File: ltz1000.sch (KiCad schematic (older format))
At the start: 62 parts, among them Q1 ZTX851, U11 ADA4522-2, U24 LT6018, U25 ADA4522-2, U26 ADA4522-1, U27 OPA140, U28 OPA140, U29 OPA140, U30 OPA140

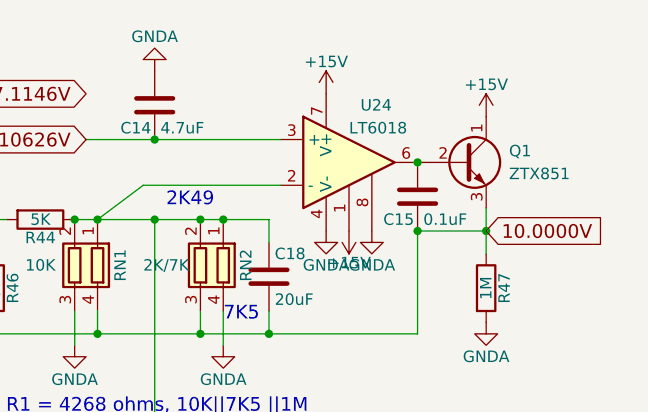
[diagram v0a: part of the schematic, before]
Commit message: Add files via upload
Updated opamps to ada4522 because they have lower bias current.
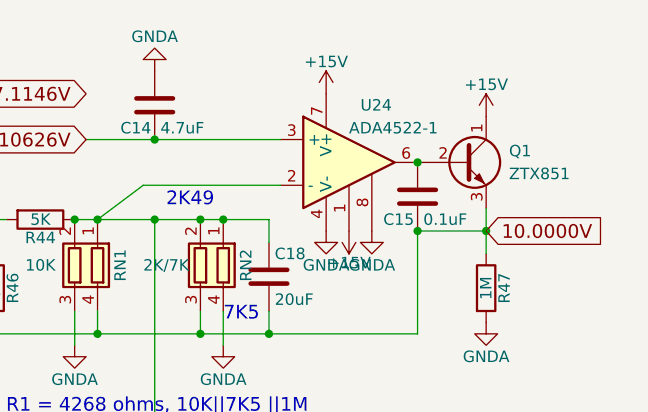
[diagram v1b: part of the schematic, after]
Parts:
- U24: value LT6018 -> ADA4522-1
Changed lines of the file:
@@
 $Descr A4 11693 8268
 encoding utf-8
-Sheet 2 5
+Sheet 2 6
 Title "DIY Differential Voltmeter.  Version 1"
 Date "2019-05-20"
@@
 NoConn ~ 2750 4800
 $Comp
-L GNDA #PWR64
+L GNDA #PWR045
 U 1 1 5B84AD0F
 P 2250 4700
-F 0 "#PWR64" H 2250 4450 50  0001 C CNN
+F 0 "#PWR045" H 2250 4450 50  0001 C CNN
 F 1 "GNDA" H 2250 4550 50  0000 C CNN
 F 2 "" H 2250 4700 50  0001 C CNN
@@
 $EndComp
 $Comp
-L +15V #PWR62
+L +15V #PWR046
 U 1 1 5B84B928
 P 2650 4200
-F 0 "#PWR62" H 2650 4050 50  0001 C CNN
+F 0 "#PWR046" H 2650 4050 50  0001 C CNN
 F 1 "+15V" H 2650 4340 50  0000 C CNN
 F 2 "" H 2650 4200 50  0001 C CNN
@@
 NoConn ~ 2750 6350
 $Comp
-L GNDA #PWR69
+L GNDA #PWR047
 U 1 1 5B84E7A7
 P 2250 6250
-F 0 "#PWR69" H 2250 6000 50  0001 C CNN
+F 0 "#PWR047" H 2250 6000 50  0001 C CNN
 F 1 "GNDA" H 2250 6100 50  0000 C CNN
 F 2 "" H 2250 6250 50  0001 C CNN
@@
 $EndComp
 $Comp
-L +15V #PWR67
+L +15V #PWR048
 U 1 1 5B84E7AE
 P 2650 5750
-F 0 "#PWR67" H 2650 5600 50  0001 C CNN
+F 0 "#PWR048" H 2650 5600 50  0001 C CNN
 F 1 "+15V" H 2650 5890 50  0000 C CNN
 F 2 "" H 2650 5750 50  0001 C CNN
@@
 NoConn ~ 6400 4700
 $Comp
-L GNDA #PWR63
+L GNDA #PWR049
 U 1 1 5B84EA99
 P 5900 4600
-F 0 "#PWR63" H 5900 4350 50  0001 C CNN
+F 0 "#PWR049" H 5900 4350 50  0001 C CNN
 F 1 "GNDA" H 5900 4450 50  0000 C CNN
 F 2 "" H 5900 4600 50  0001 C CNN
@@
 $EndComp
 $Comp
-L +15V #PWR61
+L +15V #PWR050
 U 1 1 5B84EAA0
 P 6300 4100
-F 0 "#PWR61" H 6300 3950 50  0001 C CNN
+F 0 "#PWR050" H 6300 3950 50  0001 C CNN
 F 1 "+15V" H 6300 4240 50  0000 C CNN
 F 2 "" H 6300 4100 50  0001 C CNN
@@
 NoConn ~ 6400 6400
 $Comp
-L GNDA #PWR70
+L GNDA #PWR051
 U 1 1 5B84EADB
 P 5900 6300
-F 0 "#PWR70" H 5900 6050 50  0001 C CNN
+F 0 "#PWR051" H 5900 6050 50  0001 C CNN
 F 1 "GNDA" H 5900 6150 50  0000 C CNN
 F 2 "" H 5900 6300 50  0001 C CNN
@@
 $EndComp
 $Comp
-L +15V #PWR68
+L +15V #PWR052
 U 1 1 5B84EAE2
 P 6300 5800
-F 0 "#PWR68" H 6300 5650 50  0001 C CNN
+F 0 "#PWR052" H 6300 5650 50  0001 C CNN
 F 1 "+15V" H 6300 5940 50  0000 C CNN
 F 2 "" H 6300 5800 50  0001 C CNN
@@
 $EndComp
 $Comp
-L GNDA #PWR50
+L GNDA #PWR053
 U 1 1 5B92B409
 P 1750 1750
-F 0 "#PWR50" H 1750 1500 50  0001 C CNN
+F 0 "#PWR053" H 1750 1500 50  0001 C CNN
 F 1 "GNDA" H 1750 1600 50  0000 C CNN
 F 2 "" H 1750 1750 50  0001 C CNN
@@
 $EndComp
 $Comp
-L GNDA #PWR53
+L GNDA #PWR054
 U 1 1 5B92B41E
 P 4250 1850
-F 0 "#PWR53" H 4250 1600 50  0001 C CNN
+F 0 "#PWR054" H 4250 1600 50  0001 C CNN
 F 1 "GNDA" H 4250 1700 50  0000 C CNN
 F 2 "" H 4250 1850 50  0001 C CNN
@@
 $EndComp
 $Comp
-L GNDA #PWR51
+L GNDA #PWR055
 U 1 1 5B940C92
 P 2200 1850
-F 0 "#PWR51" H 2200 1600 50  0001 C CNN
+F 0 "#PWR055" H 2200 1600 50  0001 C CNN
 F 1 "GNDA" H 2200 1700 50  0000 C CNN
 F 2 "" H 2200 1850 50  0001 C CNN
@@
 $EndComp
 $Comp
-L +15V #PWR45
+L +15V #PWR056
 U 1 1 5B941207
 P 2200 1250
-F 0 "#PWR45" H 2200 1100 50  0001 C CNN
+F 0 "#PWR056" H 2200 1100 50  0001 C CNN
 F 1 "+15V" H 2200 1390 50  0000 C CNN
 F 2 "" H 2200 1250 50  0001 C CNN
@@
 $EndComp
 $Comp
-L +15V #PWR46
+L +15V #PWR057
 U 1 1 5B99A2E8
 P 6400 1250
-F 0 "#PWR46" H 6400 1100 50  0001 C CNN
+F 0 "#PWR057" H 6400 1100 50  0001 C CNN
 F 1 "+15V" H 6400 1390 50  0000 C CNN
 F 2 "" H 6400 1250 50  0001 C CNN
@@
 $EndComp
 $Comp
-L GNDA #PWR54
+L GNDA #PWR058
 U 1 1 5B99A3CA
 P 6400 1850
-F 0 "#PWR54" H 6400 1600 50  0001 C CNN
+F 0 "#PWR058" H 6400 1600 50  0001 C CNN
 F 1 "GNDA" H 6400 1700 50  0000 C CNN
 F 2 "" H 6400 1850 50  0001 C CNN
@@
 $EndComp
 $Comp
-L GNDA #PWR56
+L GNDA #PWR059
 U 1 1 5B99C24F
 P 5850 2200
-F 0 "#PWR56" H 5850 1950 50  0001 C CNN
+F 0 "#PWR059" H 5850 1950 50  0001 C CNN
 F 1 "GNDA" H 5850 2050 50  0000 C CNN
 F 2 "" H 5850 2200 50  0001 C CNN
@@
 $EndComp
 $Comp
-L GNDA #PWR59
+L GNDA #PWR060
 U 1 1 5B99E1F3
 P 5550 2600
-F 0 "#PWR59" H 5550 2350 50  0001 C CNN
+F 0 "#PWR060" H 5550 2350 50  0001 C CNN
 F 1 "GNDA" H 5550 2450 50  0000 C CNN
 F 2 "" H 5550 2600 50  0001 C CNN
@@
 $EndComp
 $Comp
-L GNDA #PWR52
+L GNDA #PWR061
 U 1 1 5BE3AEC6
 P 3850 1850
-F 0 "#PWR52" H 3850 1600 50  0001 C CNN
+F 0 "#PWR061" H 3850 1600 50  0001 C CNN
 F 1 "GNDA" H 3850 1700 50  0000 C CNN
 F 2 "" H 3850 1850 50  0001 C CNN
@@
 P 9600 1400
 F 0 "U24" H 9650 1650 50  0000 L CNN
-F 1 "LT6018" H 9600 1550 50  0000 L CNN
+F 1 "ADA4522-1" H 9600 1550 50  0000 L CNN
 F 2 "" H 9650 1450 50  0001 C CNN
 F 3 "" H 9650 1550 50  0001 C CNN
@@
 $EndComp
 $Comp
-L +15V #PWR43
+L +15V #PWR062
 U 1 1 5BEB7DD3
 P 9500 1100
-F 0 "#PWR43" H 9500 950 50  0001 C CNN
+F 0 "#PWR062" H 9500 950 50  0001 C CNN
 F 1 "+15V" H 9500 1240 50  0000 C CNN
 F 2 "" H 9500 1100 50  0001 C CNN
@@
 $EndComp
 $Comp
-L GNDA #PWR47
+L GNDA #PWR063
 U 1 1 5BEB7DD9
 P 9500 1700
-F 0 "#PWR47" H 9500 1450 50  0001 C CNN
+F 0 "#PWR063" H 9500 1450 50  0001 C CNN
 F 1 "GNDA" H 9500 1550 50  0000 C CNN
 F 2 "" H 9500 1700 50  0001 C CNN
@@
 $EndComp
 $Comp
-L GNDA #PWR58
+L GNDA #PWR064
 U 1 1 5BEB7DED
 P 9050 2200
-F 0 "#PWR58" H 9050 1950 50  0001 C CNN
+F 0 "#PWR064" H 9050 1950 50  0001 C CNN
 F 1 "GNDA" H 9050 2050 50  0000 C CNN
 F 2 "" H 9050 2200 50  0001 C CNN
@@
 $EndComp
 $Comp
-L GNDA #PWR57
+L GNDA #PWR065
 U 1 1 5BEB887E
 P 8400 2200
-F 0 "#PWR57" H 8400 1950 50  0001 C CNN
+F 0 "#PWR065" H 8400 1950 50  0001 C CNN
 F 1 "GNDA" H 8400 2050 50  0000 C CNN
 F 2 "" H 8400 2200 50  0001 C CNN
@@
 $EndComp
 $Comp
-L +15V #PWR44
+L +15V #PWR066
 U 1 1 5C1C927E
 P 10200 1200
-F 0 "#PWR44" H 10200 1050 50  0001 C CNN
+F 0 "#PWR066" H 10200 1050 50  0001 C CNN
 F 1 "+15V" H 10200 1340 50  0000 C CNN
 F 2 "" H 10200 1200 50  0001 C CNN
@@
 $EndComp
 $Comp
-L GNDA #PWR55
+L GNDA #PWR067
 U 1 1 5C1C94C5
 P 10200 2100
-F 0 "#PWR55" H 10200 1850 50  0001 C CNN
+F 0 "#PWR067" H 10200 1850 50  0001 C CNN
 F 1 "GNDA" H 10200 1950 50  0000 C CNN
 F 2 "" H 10200 2100 50  0001 C CNN
@@
 Connection ~ 9900 1400
 $Comp
-L +15V #PWR48
+L +15V #PWR068
 U 1 1 5C1D3F28
 P 9600 1700
-F 0 "#PWR48" H 9600 1550 50  0001 C CNN
+F 0 "#PWR068" H 9600 1550 50  0001 C CNN
 F 1 "+15V" H 9600 1840 50  0000 C CNN
 F 2 "" H 9600 1700 50  0001 C CNN
@@
 $EndComp
 $Comp
-L GNDA #PWR49
+L GNDA #PWR069
 U 1 1 5C1D3FE7
 P 9700 1700
-F 0 "#PWR49" H 9700 1450 50  0001 C CNN
+F 0 "#PWR069" H 9700 1450 50  0001 C CNN
 F 1 "GNDA" H 9700 1550 50  0000 C CNN
 F 2 "" H 9700 1700 50  0001 C CNN
@@
 $EndComp
 $Comp
-L GNDA #PWR42
+L GNDA #PWR070
 U 1 1 5C1D4420
 P 8750 1000
-F 0 "#PWR42" H 8750 750 50  0001 C CNN
+F 0 "#PWR070" H 8750 750 50  0001 C CNN
 F 1 "GNDA" H 8750 850 50  0000 C CNN
 F 2 "" H 8750 1000 50  0001 C CNN
@@
 Connection ~ 8750 1650
 $Comp
-L GNDA #PWR60
+L GNDA #PWR071
 U 1 1 5C4936C7
 P 8750 3000
-F 0 "#PWR60" H 8750 2750 50  0001 C CNN
+F 0 "#PWR071" H 8750 2750 50  0001 C CNN
 F 1 "GNDA" H 8750 2850 50  0000 C CNN
 F 2 "" H 8750 3000 50  0001 C CNN

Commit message: Add files via upload
Version 1.6
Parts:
- removed C13: 1u, symbol C
- removed C16, C22, C23, C26, C27: 4.7uF, symbol C
- removed C17, C19: 20uF, symbol C
- removed C20, C21, C24, C25: 10uF, symbol C
- removed Q1: ZTX851, symbol Q_NPN_CBE
- removed R34, R35, R36, R39, R42, R50, R51, R54, R57, R60, R63, R64: 2K, symbol R
- removed R37: 30K, symbol R
- removed R38: 20K, symbol R
- removed R40: 10, symbol R
- removed R41: 2500, symbol R
- removed R45: 5000, symbol R
- removed R47, R53, R56, R59, R62: 1M, symbol R
- removed R48: 150K, symbol R
- removed R52, R55, R58, R61: 75K, symbol R
- removed RN3: 10K, symbol R_Pack02
- removed RV1: 20K 1280G, symbol POT
- removed RV2: 500, symbol POT
- removed TH1: Thermistor 500ohm, symbol Thermistor
- removed U11, U25: ADA4522-2, symbol ADA4075
- removed U26: ADA4522-1, symbol OP07
- removed U27, U28, U29, U30: OPA140, symbol OP07
- added R5: 20K, symbol R
- added R6, R7: 10K, symbol R
- added U2: LT1010H, symbol LT1010H
- U1: renamed from U24; value ADA4522-1 -> OPA189
- renumbered C14 to C1, C18 to C2, C15 to C3, R43 to R1, R46 to R2, R44 to R3, R49 to R4, RV3 to RV1
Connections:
- net labels added: 2.500V, 5.000V, 7.1071830V
- net labels removed: -15V, 5.0000V, 7.10626V, 7.1146V, KX1-brown, PX3-red, PX4-purple, PX5-orange, PX6-grey, PX7-yellow, PX8-white, Temperature, VRefFiltered-1, VRefFiltered-2, VRefFiltered-3, VRefFiltered-4
- wire segments 95 -> 24
- no-connect marks 10 -> 3
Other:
- note added: "AE HZT"
- note added: "Thermally coupled"
- note added: "Z201T\n"
- note removed: "<-- 2112 ohms -->"
- note removed: "Vishay DSMZ 3ppm\n0.1ppm tracking"
- moved on the sheet: C1, C2, C3, R1, R2, R3, R4, RN1, RN2, RV1, U1
